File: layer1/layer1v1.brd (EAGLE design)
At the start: 100 x 80 mm, 7 parts, among them U1 microSD, U2 DS3234

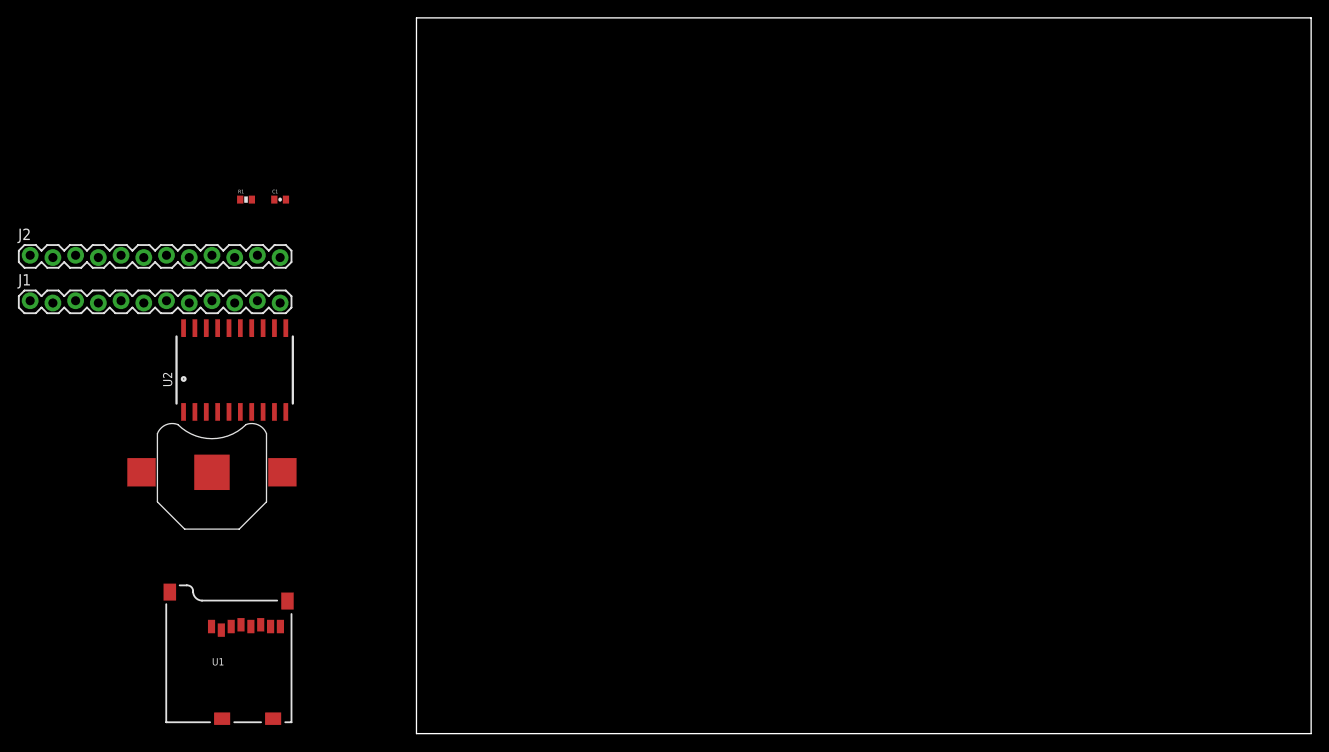
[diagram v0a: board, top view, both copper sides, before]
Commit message: added batteri connection to board
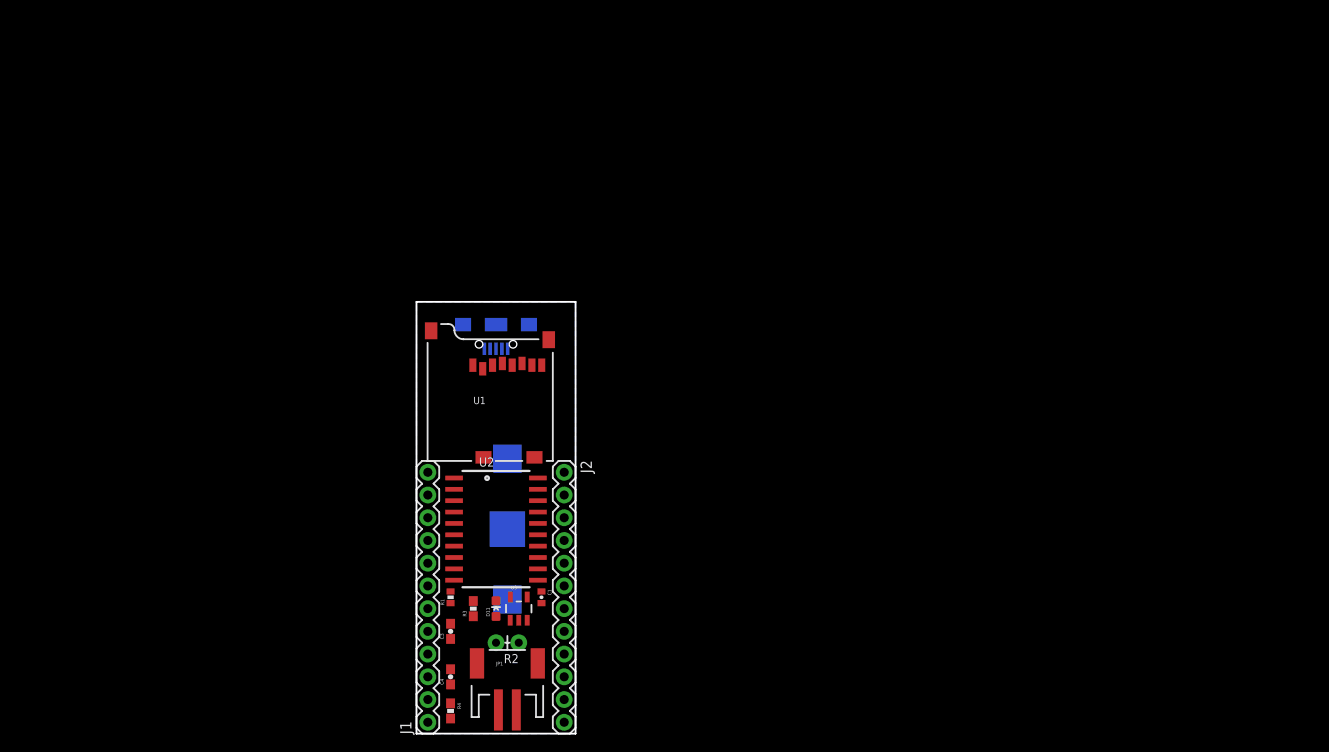
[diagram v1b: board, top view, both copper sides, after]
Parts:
- added C3, C4: 4.7uF, SparkFun-Capacitors:0603-CAP
- added D11: RED, SparkFun-LED:LED-0603
- added JP1: JST, SparkFun-Connectors:JST-2-SMD
- added JP9: Micro USB, SparkFun-Connectors:USB-AB-MICRO-SMD_V03
- added R2: (no value), SparkFun-Resistors:AXIAL-0.1EZ
- added R3: 330, SparkFun-Resistors:0603-RES
- added R4: 2.0k, SparkFun-Resistors:0603-RES
- added U3: MCP73831, SparkFun-PowerIC:SOT23-5
- J1, J2: device SparkFun-Connectors:1X12_LOCK -> SparkFun-Connectors:1X12
- moved J1 64.7 mm to (1.27, 1.27), turned to 90 degrees
- moved J2 64.4 mm to (16.5, 29.2), turned to 270 degrees
- moved C1 53.2 mm to (14.0, 15.2), turned to 270 degrees
- moved R1 50.0 mm to (3.81, 15.2), turned to 90 degrees
- moved U1 41.3 mm to (15.2, 30.5)
- moved U2 34.2 mm to (8.89, 22.9), turned to 270 degrees
- moved BAT1 33.6 mm to (10.2, 22.9), flipped to the bottom, turned to 90 degrees
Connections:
- new net N$3: D11.A, R3.1
- new net PROG: R2.P$2, R4.1, U3.5
- new net STAT: D11.C, U3.1
- new net VIN: C3.1, JP9.VBUS1, R3.2, U3.4
- new net V_RAW: C4.1, J2.1, JP1.2, U3.3
- net GND: now also C3.2, C4.2, J2.2, JP1.1, JP9.GND1, R2.P$1, R4.2, U3.2; no longer J2.11
- net MISO: now also J2.10; no longer J2.3
- net MOSI: now also J2.11; no longer J2.2
- net SCK: now also J2.9; no longer J2.4
- net SD_CS: now also J2.12; no longer J2.1
- net VCC: now also J2.4; no longer J2.9
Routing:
- added copper zone on layer 16, net N$1
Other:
- board size 100 x 80 mm -> 17.8 x 48.3 mm
